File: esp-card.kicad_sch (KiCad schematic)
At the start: 12 parts, among them J1 Conn_01x01_Socket, U1 XC6206P332MR, U2 ESP32-C3FH4, U3 TYPE_C-CQ-111PWB, X1 CF4040M00015001

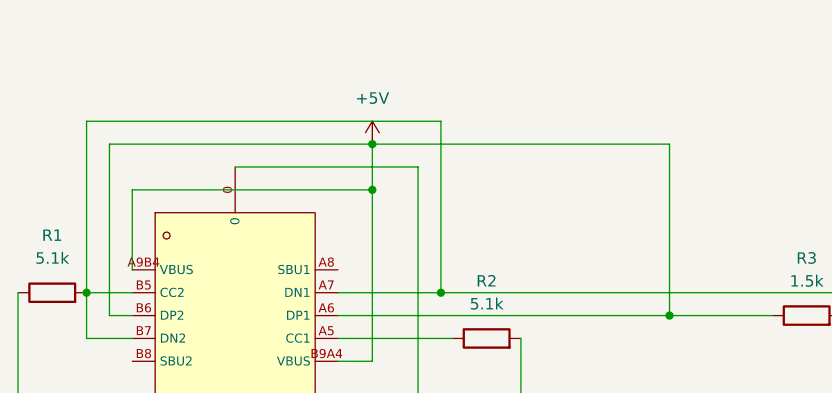
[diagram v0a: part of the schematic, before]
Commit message: Fix accidental connection of D+ and VBUS
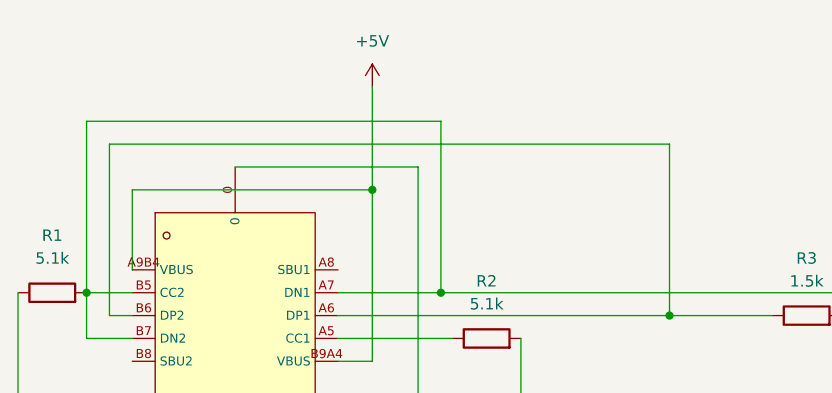
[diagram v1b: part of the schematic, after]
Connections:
- net +5V: no longer R3.1, U3.A6 (DP1), U3.B6 (DP2)
- new net: R3.1, U3.A6 (DP1), U3.B6 (DP2)
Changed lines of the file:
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@@
-	)
-	(junction
-		(at 57.15 33.02)
-		(diameter 0)
-		(color 0 0 0 0)
 	)
 	(junction
@@
 	(wire
 		(pts
-			(xy 57.15 38.1) (xy 57.15 33.02)
+			(xy 57.15 26.67) (xy 57.15 38.1)
 		)
 		(stroke
@@
 	(wire
 		(pts
-			(xy 27.94 33.02) (xy 57.15 33.02)
-		)
-		(stroke
-			(width 0)
-			(type default)
-		)
-	)
-	(wire
-		(pts
 			(xy 62.23 35.56) (xy 62.23 63.5)
 		)
@@
 	(wire
 		(pts
-			(xy 57.15 33.02) (xy 90.17 33.02)
+			(xy 27.94 33.02) (xy 90.17 33.02)
 		)
 		(stroke
@@
 	(symbol
 		(lib_id "power:+5V")
-		(at 57.15 33.02 0)
+		(at 57.15 26.67 0)
 		(unit 1)
 		(exclude_from_sim no)
@@
 		(fields_autoplaced yes)
 		(property "Reference" "#PWR02"
-			(at 57.15 36.83 0)
+			(at 57.15 30.48 0)
 			(effects
 				(font
@@
 		)
 		(property "Value" "+5V"
-			(at 57.15 27.94 0)
+			(at 57.15 21.59 0)
 			(effects
 				(font
@@
 		)
 		(property "Footprint" ""
-			(at 57.15 33.02 0)
+			(at 57.15 26.67 0)
 			(effects
 				(font
@@
 		)
 		(property "Datasheet" ""
-			(at 57.15 33.02 0)
+			(at 57.15 26.67 0)
 			(effects
 				(font
@@
 		)
 		(property "Description" "Power symbol creates a global label with name \"+5V\""
-			(at 57.15 33.02 0)
-			(effects
-				(font
+			(at 57.15 26.67 0)
+			(effects
+				(font

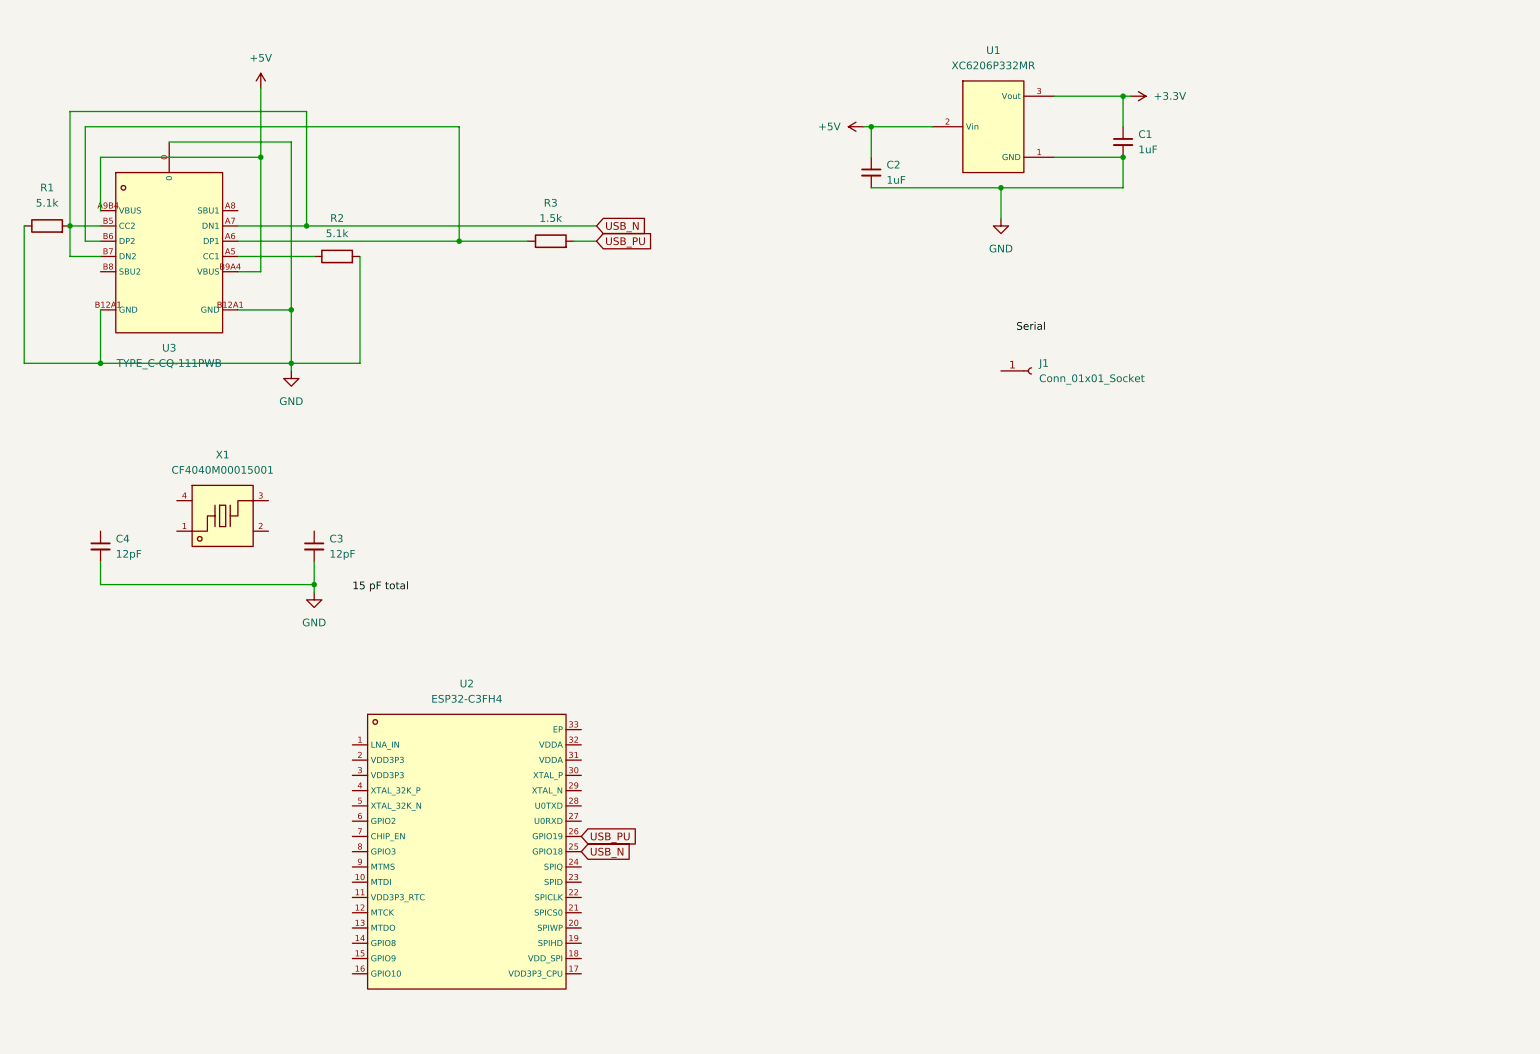
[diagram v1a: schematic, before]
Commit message: Hook up clock, UART
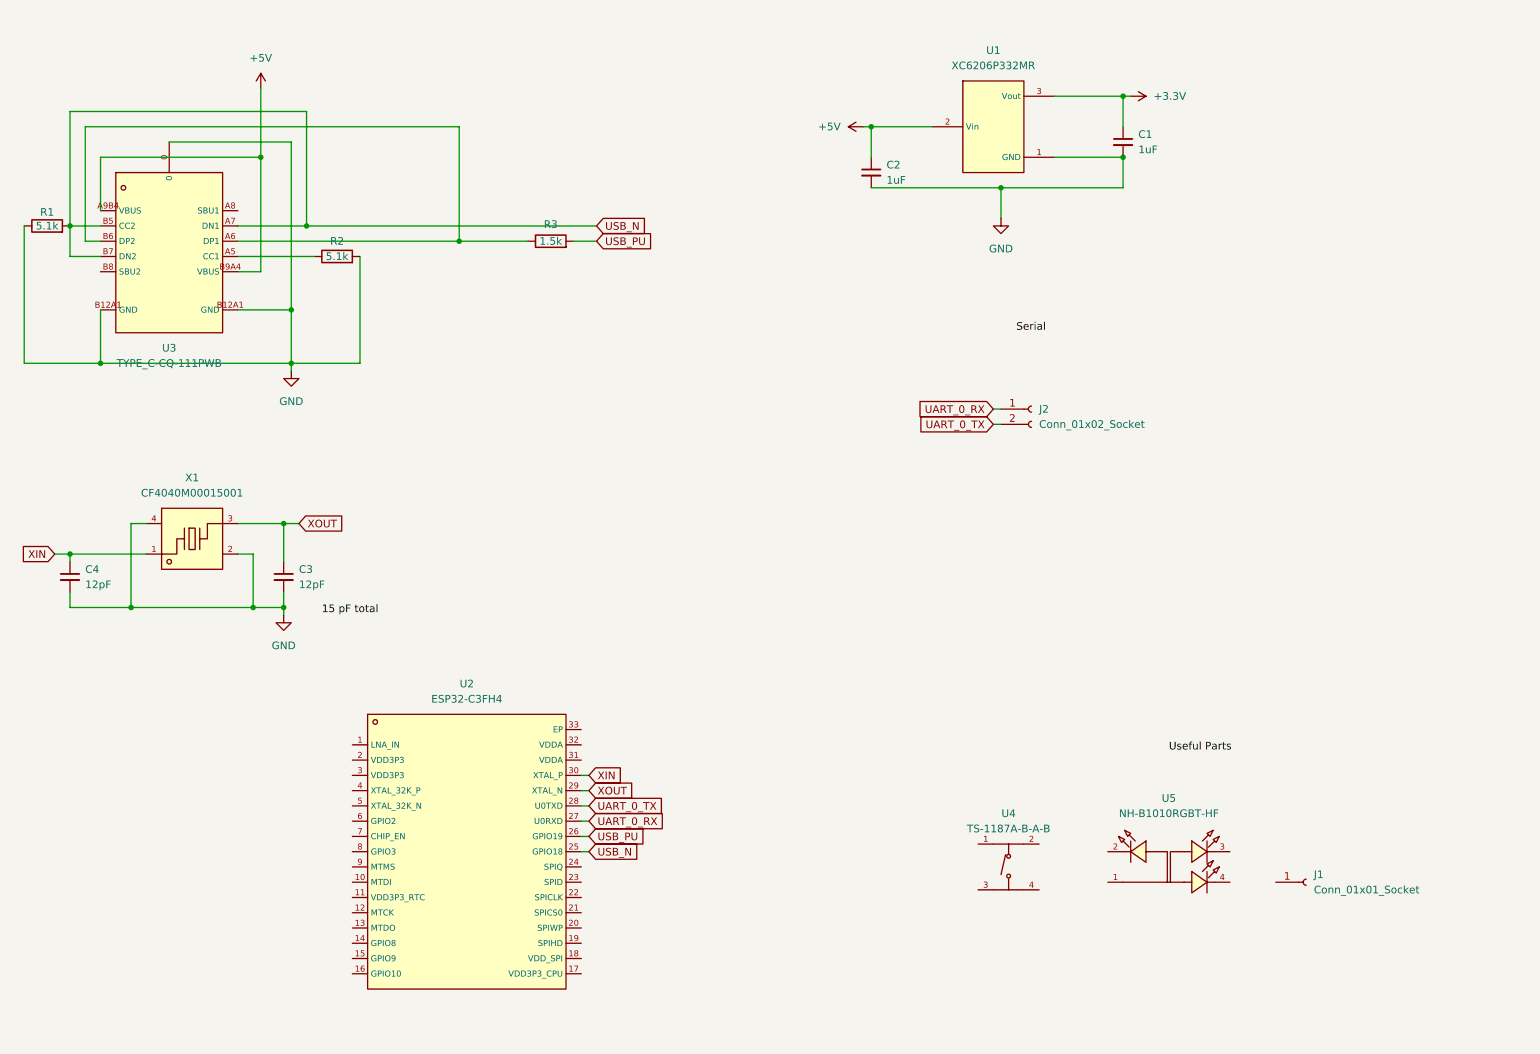
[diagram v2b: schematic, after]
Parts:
- added J2: Conn_01x02_Socket, symbol Connector:Conn_01x02_Socket
- added U4: TS-1187A-B-A-B, footprint:SW-SMD_4P-L5.1-W5.1-P3.70-LS6.5-TL-2, symbol TS-1187A-B-A-B:TS-1187A-B-A-B
- added U5: NH-B1010RGBT-HF, footprint:LED-ARRAY-SMD_4P-L1.0-W1.0-TR_NH-B1010RGBT, symbol NH-B1010RGBT-HF:NH-B1010RGBT-HF
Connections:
- net GND: now also X1.2 (GND), X1.4 (GND)
- net XIN: now reaches C4.1
- net XIN: now also U2.30 (XTAL_P), X1.1
- net XOUT: now reaches X1.3
- net XOUT: now also C3.1, U2.29 (XTAL_N)
- net UART_0_RX: now reaches U2.27 (U0RXD)
- net UART_0_RX: now also J2.1 (Pin_1)
- net UART_0_TX: now reaches U2.28 (U0TXD)
- net UART_0_TX: now also J2.2 (Pin_2)
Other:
- moved on the sheet: C3, C4, J1, X1

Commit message: added labels and figured out RGB charlieplexing
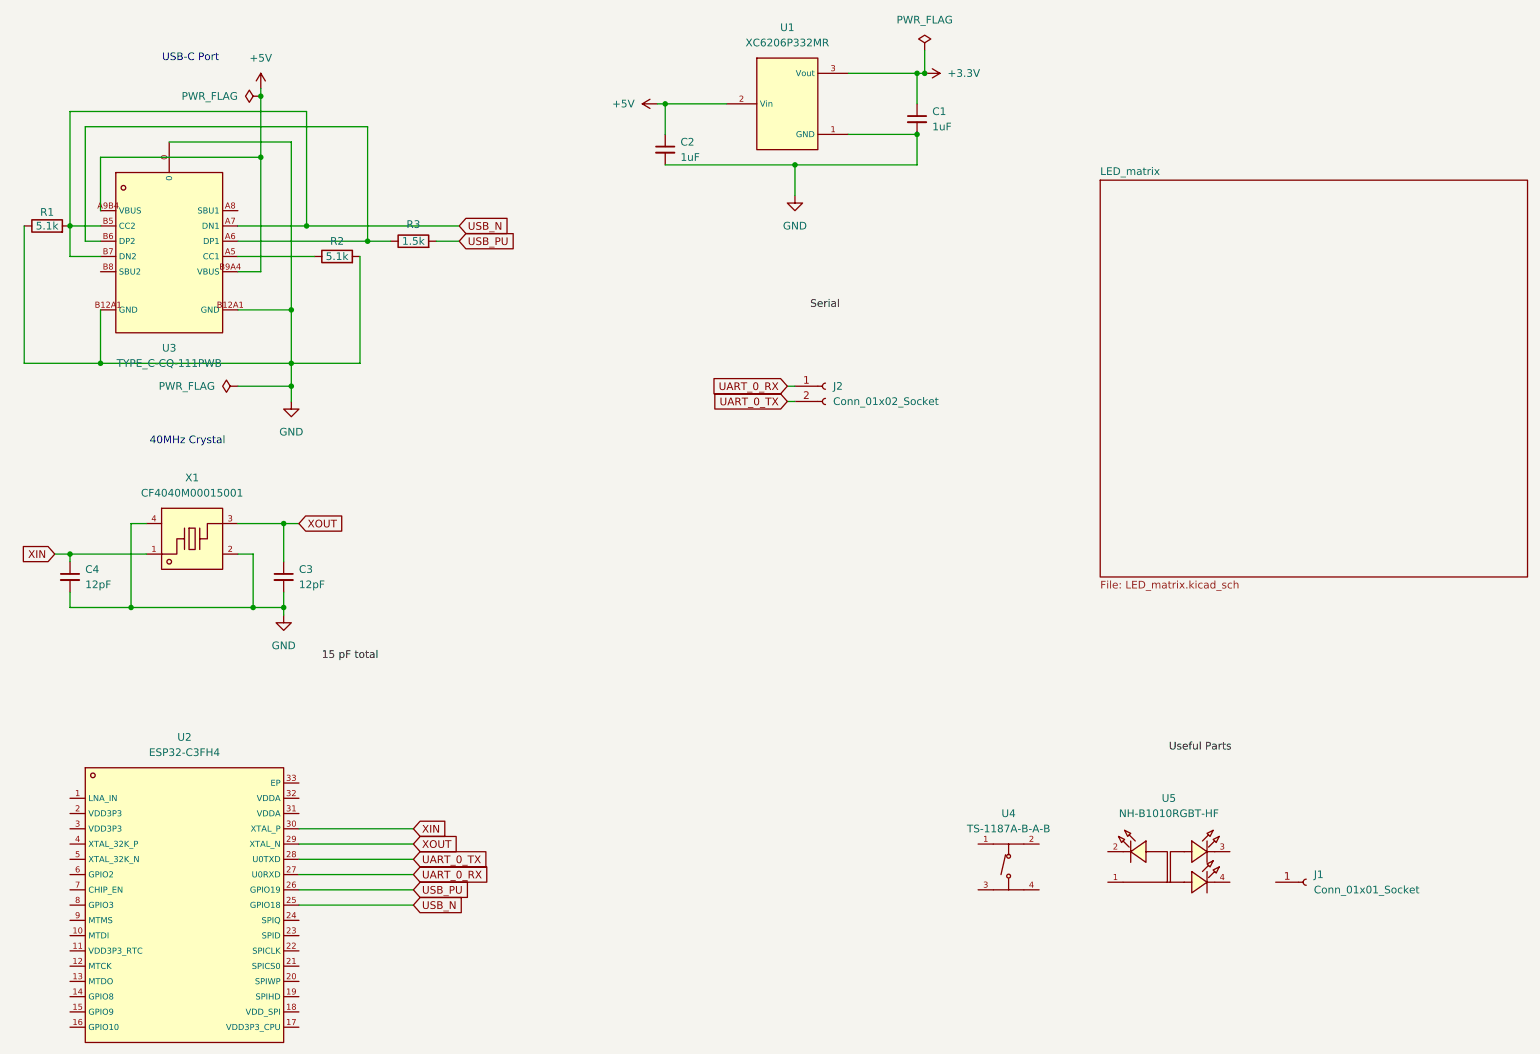
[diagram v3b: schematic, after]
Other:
- added sheet LED_matrix (LED_matrix.kicad_sch)
- note added: "40MHz Crystal"
- note added: "USB-C Port"
- moved on the sheet: C1, C2, J2, R3, U1, U2

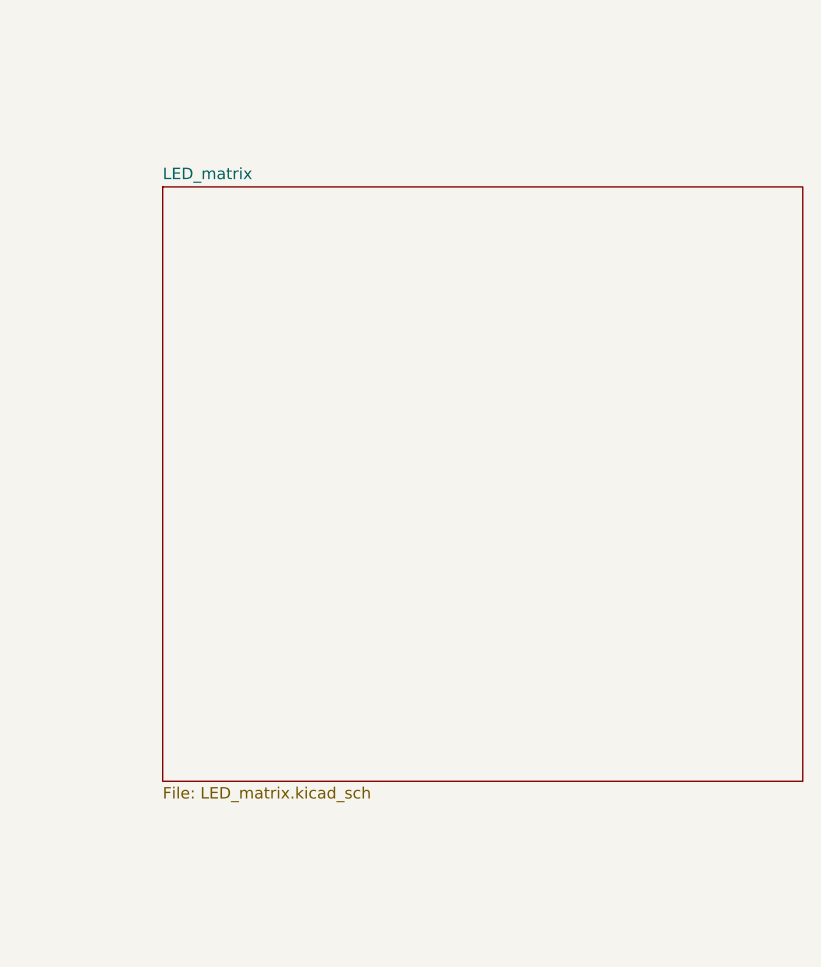
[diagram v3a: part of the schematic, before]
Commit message: fix: led matrix clean up with bus notation
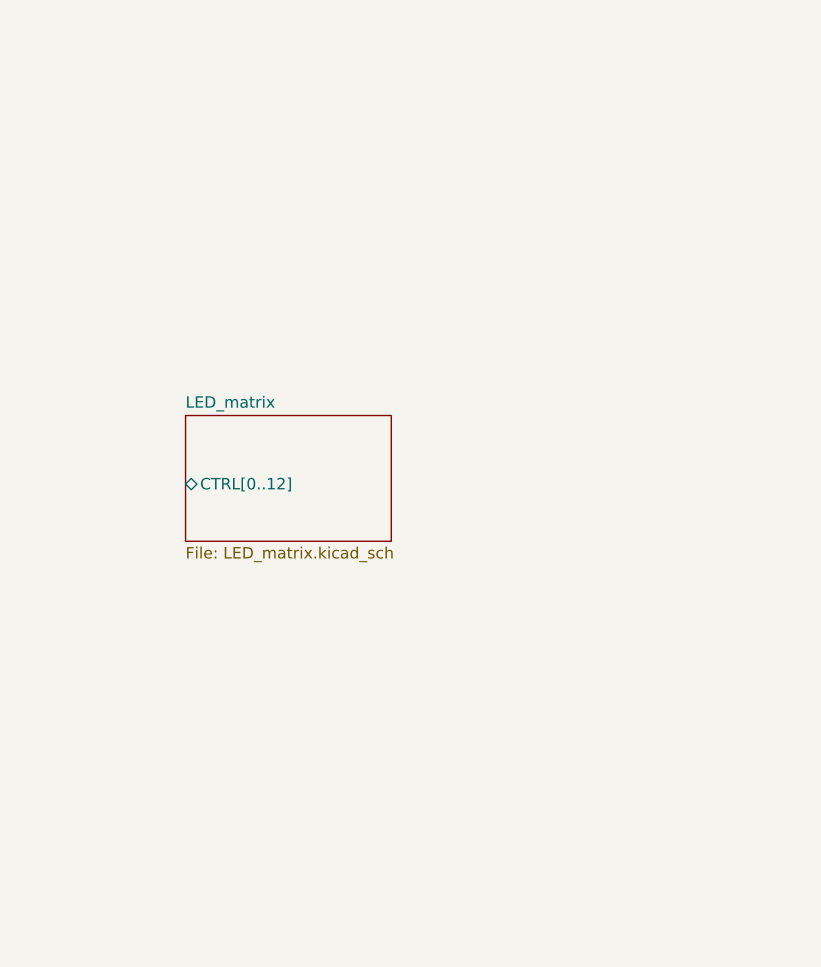
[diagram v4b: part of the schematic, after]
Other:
- sheet LED_matrix ports: added CTRL[0..12]; removed none
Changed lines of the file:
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@@
 	)
 	(sheet
-		(at 196.85 41.91)
-		(size 71.12 66.04)
+		(at 199.39 67.31)
+		(size 22.86 13.97)
 		(fields_autoplaced yes)
 		(stroke
@@
 		)
 		(property "Sheetname" "LED_matrix"
-			(at 196.85 41.1984 0)
+			(at 199.39 66.5984 0)
 			(effects
 				(font
@@
 		)
 		(property "Sheetfile" "LED_matrix.kicad_sch"
-			(at 196.85 108.5346 0)
+			(at 199.39 81.8646 0)
 			(effects
 				(font
@@
 			)
 		)
+		(pin "CTRL[0..12]" tri_state
+			(at 199.39 74.93 180)
+			(effects
+				(font
+					(size 1.27 1.27)
+				)
+				(justify left)
+			)
+		)
